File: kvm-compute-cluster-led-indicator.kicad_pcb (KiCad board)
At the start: 2 copper layers, 90 x 32.6 mm, 27 parts, among them J1 TE_1-1734248-5_FLEX, U1 PCA9685BS,118

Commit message: Add OSHW Logo
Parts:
- added N2: oshw_logo, antmicro-footprints:OSHW-Logo_5.7x6mm_SilkScreen, F.Cu at (117.1, 79.8)
- N1: footprint antmicro-footprints:antmicro-logo_scaled_12mm_silk -> antmicro-footprints:antmicro-logo_scaled_15mm_silk
- moved N1 10.8 mm to (131.7, 79.2)
- moved D2 0.40 mm to (106.9, 84.0)
- moved D3 0.40 mm to (106.9, 79.3)
- moved D4 0.40 mm to (106.9, 74.6)
- moved R16 0.40 mm to (104.6, 72.3)
- moved R17 0.40 mm to (104.6, 70.8)
- moved R18 0.40 mm to (104.6, 69.2)
- moved R2 0.40 mm to (104.6, 90.6)
- moved D1 0.40 mm to (106.9, 88.7)
- moved D5 0.40 mm to (106.9, 70.0)
- moved R1 0.40 mm to (109.6, 68.7)
- moved R10 0.40 mm to (104.6, 81.5)
- moved R11 0.40 mm to (104.6, 79.9)
- moved R12 0.40 mm to (104.6, 78.4)
- moved R13 0.40 mm to (104.6, 76.9)
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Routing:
- net /LED_4_B: track 9.99 -> 9.34 mm
- net Net-(D5-Pad1): track 3.68 -> 3.06 mm
- net /LED_5_G: track 6.34 -> 5.81 mm
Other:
- board text added: "KVM cluster LED indicator Rev.1.0.0 02/2021"
- board text removed: "KVM cluster LED indicator Rev1.0.0"

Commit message: Add stiffener descriptions
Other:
- board text added: "Stiffener 0,2mm"
- board text added: "Stiffener 0,8mm"

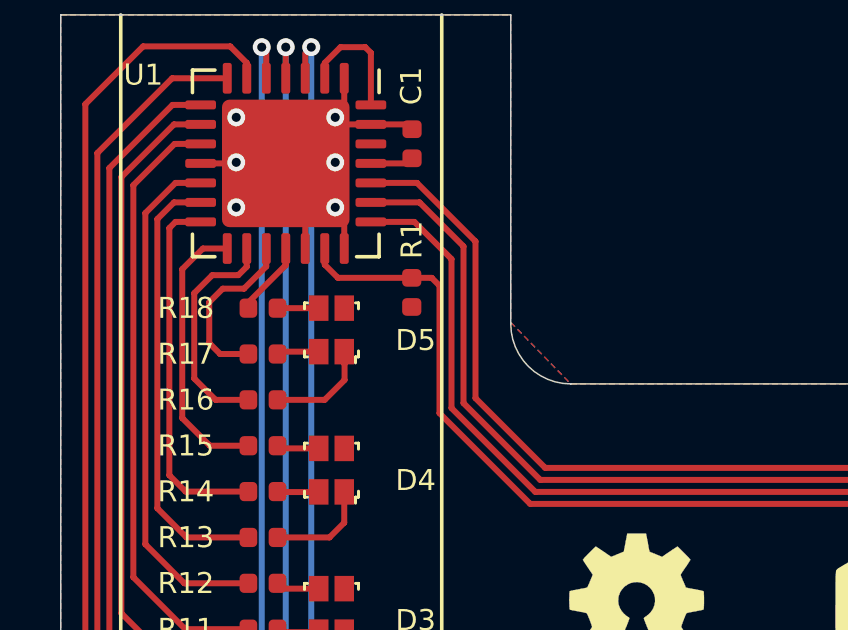
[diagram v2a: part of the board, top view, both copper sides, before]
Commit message: Add 0R DNP resistor at ~OE pin
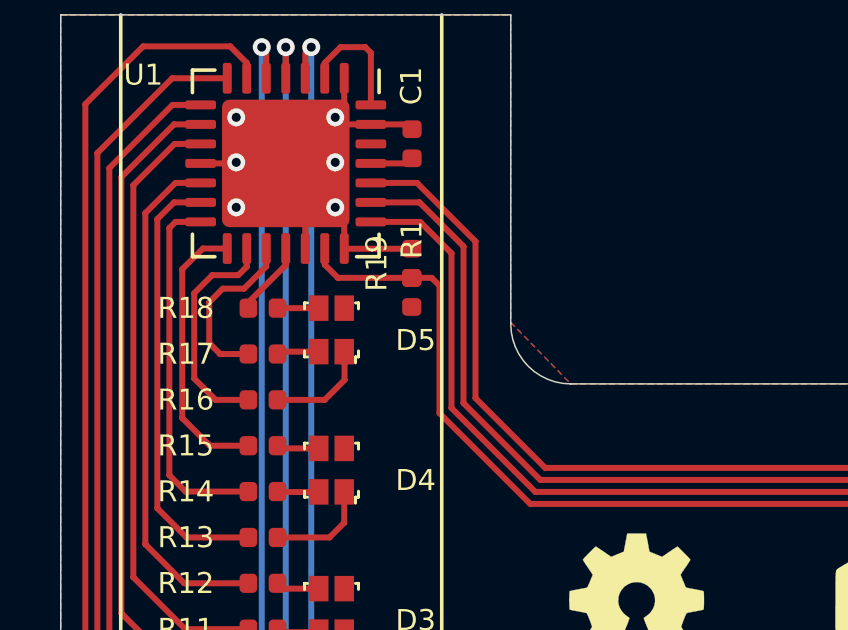
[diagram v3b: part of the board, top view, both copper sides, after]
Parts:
- added R19: R_0R_0402, antmicro-footprints:0402-res, F.Cu at (109.6, 67.7)
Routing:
- net GND: track 30.4 -> 32.7 mm

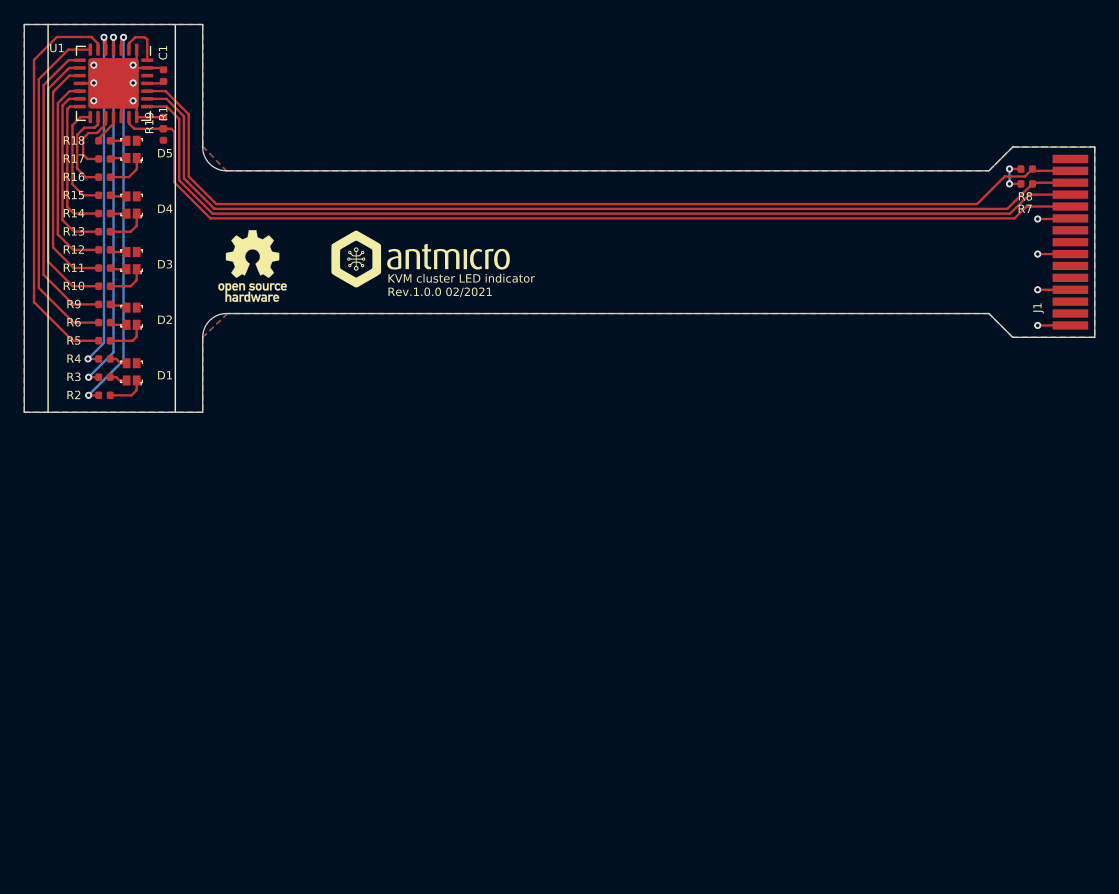
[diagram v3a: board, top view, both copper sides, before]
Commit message: Update shape and placement, reroute the PCB
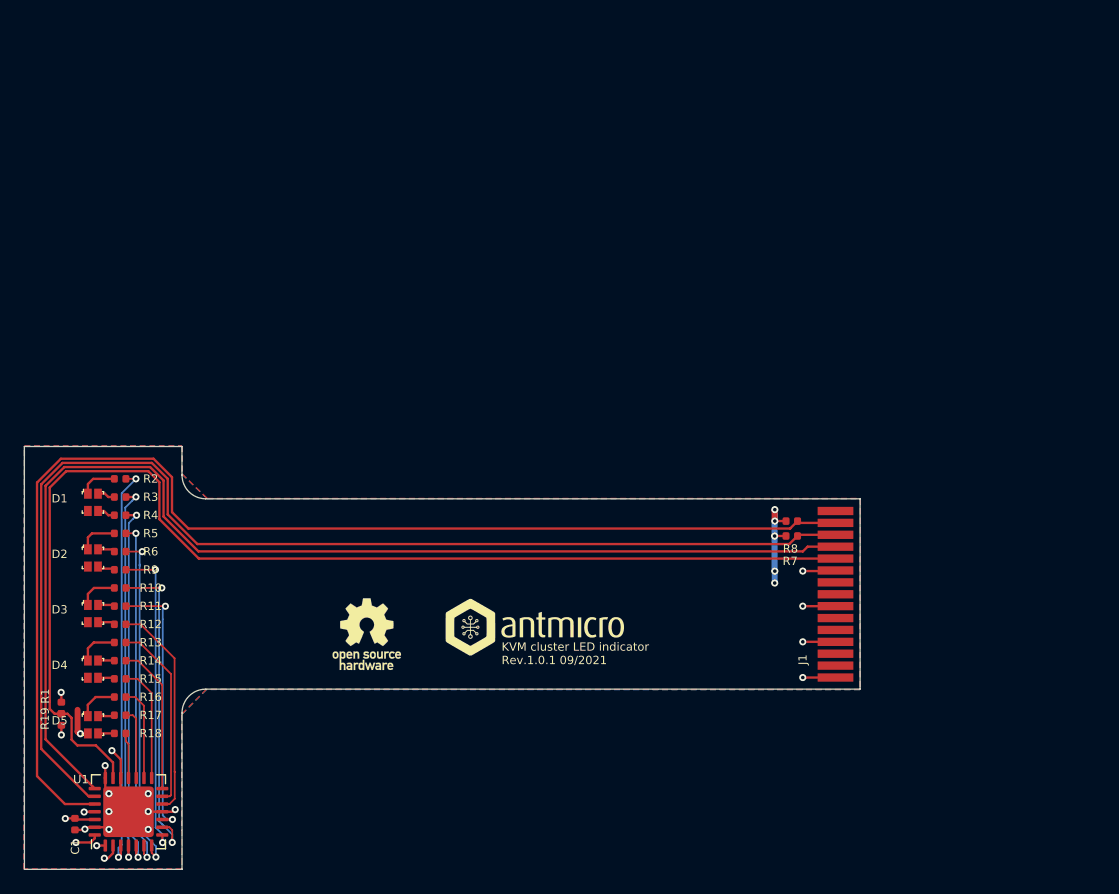
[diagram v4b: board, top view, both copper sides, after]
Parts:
- moved C1 63.4 mm to (102.2, 126.7), turned to 90 degrees
- moved U1 61.2 mm to (106.7, 125.6), turned to 90 degrees
- moved R19 50.9 mm to (101.0, 117.9), turned to 270 degrees
- moved R18 49.8 mm to (106.0, 119.0), turned to 180 degrees
- moved R1 49.0 mm to (101.0, 116.9), turned to 270 degrees
- moved D5 48.5 mm to (103.7, 118.3), turned to 0 degrees
- moved R17 46.8 mm to (106.0, 117.5), turned to 180 degrees
- moved R16 43.7 mm to (106.0, 116.0), turned to 180 degrees
- moved R15 40.7 mm to (106.0, 114.5), turned to 180 degrees
- moved D4 39.2 mm to (103.7, 113.6), turned to 0 degrees
- moved R14 37.6 mm to (106.0, 112.9), turned to 180 degrees
- moved R7 35.6 mm to (162.4, 102.5)
- moved R8 35.6 mm to (162.4, 101.2)
- moved J1 35.6 mm to (166.2, 109.3)
- moved R13 34.6 mm to (106.0, 111.4), turned to 180 degrees
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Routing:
- net /SDA: track 85.9 -> 102.9 mm
- net /SCL: track 85.4 -> 100.8 mm
- net +3V3: track 8.71 -> 23.9 mm, vias 2 -> 11
- net /CLK: track 85.0 -> 99.1 mm
- net /GPIO: track 85.9 -> 99.7 mm
- net /LED_3_R: track 22.6 -> 27.3 mm, vias 0 -> 2
- net /LED_2_R: track 34.1 -> 29.6 mm, vias 0 -> 2
- net /LED_3_G: track 20.0 -> 22.8 mm, vias 0 -> 2
- net /LED_1_B: track 29.4 -> 31.3 mm
- net /LED_1_G: track 31.3 -> 32.6 mm
- net /LED_5_B: track 2.60 -> 3.84 mm
- net /LED_4_R: track 14.8 -> 15.9 mm
- net /LED_2_B: track 25.2 -> 26.3 mm, vias 0 -> 2
- net /LED_1_R: track 33.2 -> 34.3 mm
- net /LED_3_B: track 17.3 -> 18.3 mm
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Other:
- board size 90 x 32.6 mm -> 70.3 x 35.6 mm
- net class Default: clearance 0.2 -> 0.15; trace_width 0.2 -> 0.15
- rule trace_clearance: 0.2 -> 0.15
- rule trace_min: 0.2 -> 0.11
- board text added: "KVM cluster LED indicator Rev.1.0.1 09/2021"
- board text removed: "KVM cluster LED indicator Rev.1.0.0 02/2021"

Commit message: Add minor fixes
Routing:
- net /SCL: track 100.8 -> 101.5 mm
- net /CLK: track 99.1 -> 99.7 mm
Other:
- board text added: "KVM cluster LED indicator Rev.1.0.1 10/2021"
- board text removed: "KVM cluster LED indicator Rev.1.0.1 09/2021"
